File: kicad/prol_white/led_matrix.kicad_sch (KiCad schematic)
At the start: 113 parts

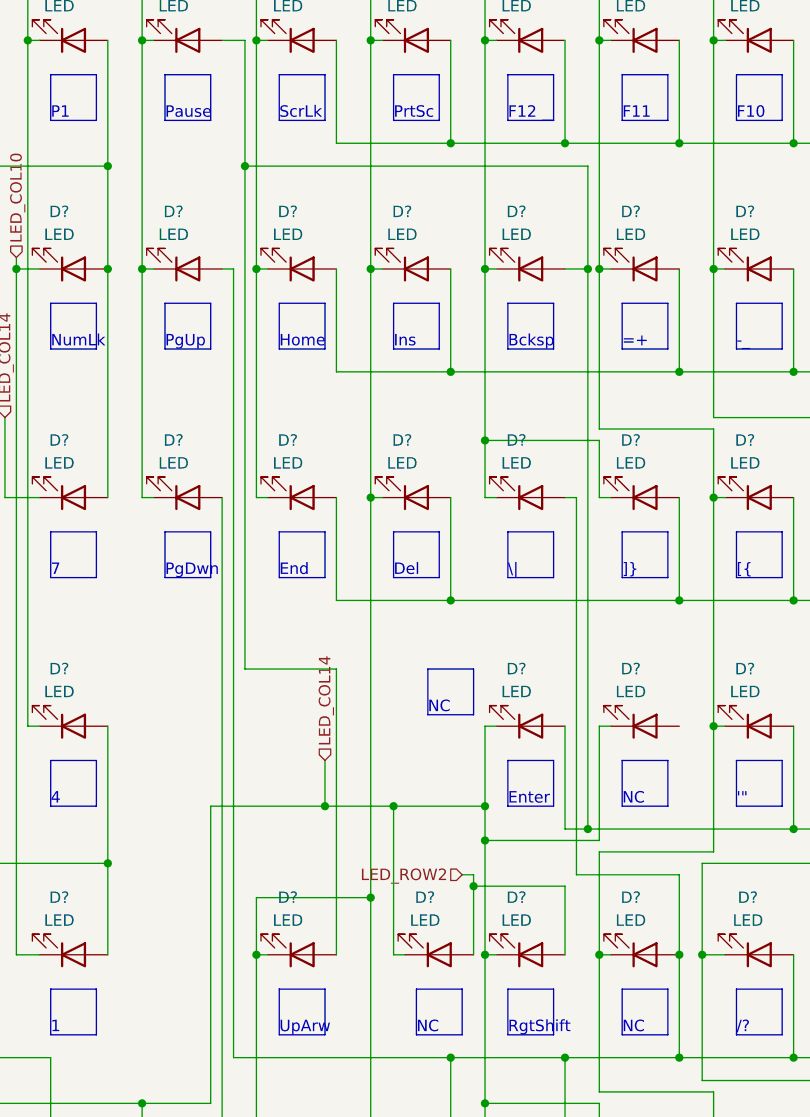
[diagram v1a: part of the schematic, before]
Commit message: kicad/prol_white: finish key matrix sheet
Used QMK debug logging to complete key matrix.
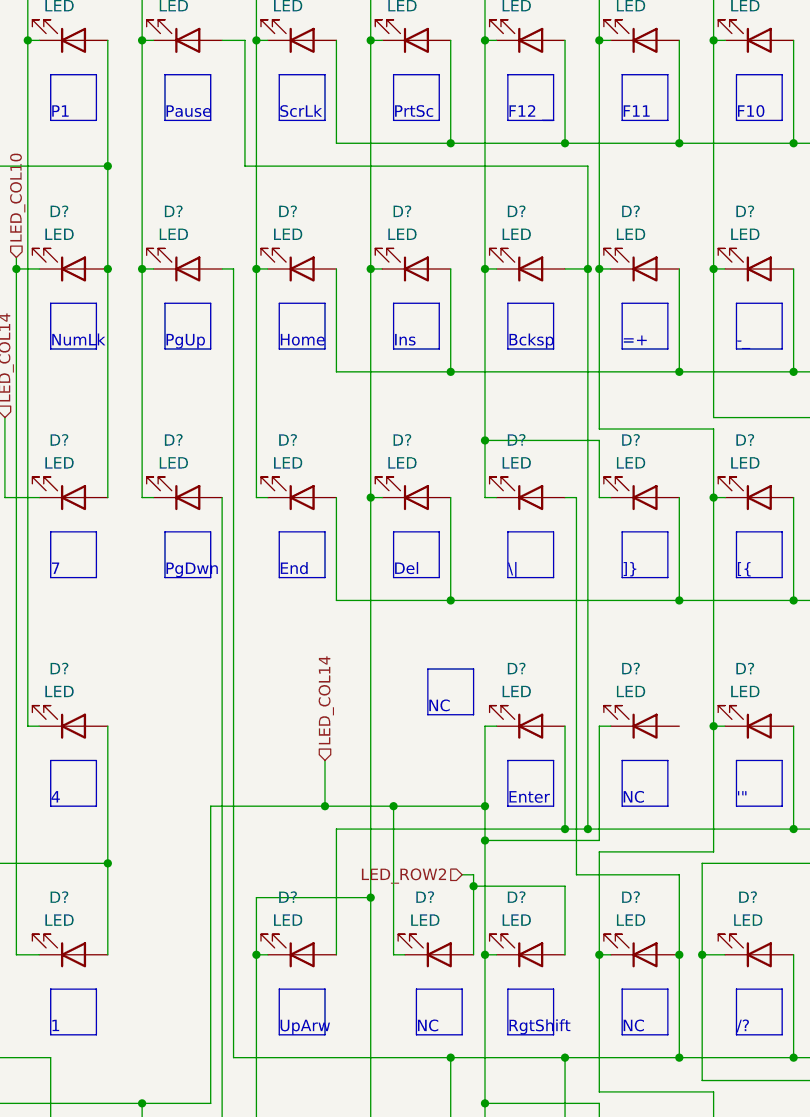
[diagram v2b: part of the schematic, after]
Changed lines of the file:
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@@
   (junction (at 140.97 173.99) (diameter 0) (color 0 0 0 0)
   )
+  (junction (at 115.57 123.19) (diameter 0) (color 0 0 0 0)
+  )
   (junction (at 217.17 111.76) (diameter 0) (color 0 0 0 0)
   )
@@
   (junction (at 246.38 86.36) (diameter 0) (color 0 0 0 0)
   )
-  (junction (at 80.01 49.53) (diameter 0) (color 0 0 0 0)
-  )
   (junction (at 119.38 60.96) (diameter 0) (color 0 0 0 0)
   )
@@
     (stroke (width 0) (type default) (color 0 0 0 0))
   )
+  (wire (pts (xy 90.17 137.16) (xy 90.17 123.19))
+    (stroke (width 0) (type default) (color 0 0 0 0))
+  )
   (wire (pts (xy 157.48 74.93) (xy 170.18 74.93))
     (stroke (width 0) (type default) (color 0 0 0 0))
@@
     (stroke (width 0) (type default) (color 0 0 0 0))
   )
-  (wire (pts (xy 90.17 105.41) (xy 90.17 137.16))
-    (stroke (width 0) (type default) (color 0 0 0 0))
-  )
   (wire (pts (xy 68.58 35.56) (xy 69.85 35.56))
     (stroke (width 0) (type default) (color 0 0 0 0))
@@
     (stroke (width 0) (type default) (color 0 0 0 0))
   )
-  (wire (pts (xy 80.01 105.41) (xy 90.17 105.41))
-    (stroke (width 0) (type default) (color 0 0 0 0))
-  )
   (polyline (pts (xy 223.52 146.05) (xy 228.6 146.05))
     (stroke (width 0) (type default) (color 0 0 0 0))
@@
     (stroke (width 0) (type default) (color 0 0 0 0))
   )
+  (wire (pts (xy 90.17 123.19) (xy 115.57 123.19))
+    (stroke (width 0) (type default) (color 0 0 0 0))
+  )
   (wire (pts (xy 195.58 86.36) (xy 196.85 86.36))
     (stroke (width 0) (type default) (color 0 0 0 0))
@@
     (stroke (width 0) (type default) (color 0 0 0 0))
   )
-  (wire (pts (xy 80.01 49.53) (xy 80.01 105.41))
-    (stroke (width 0) (type default) (color 0 0 0 0))
-  )
